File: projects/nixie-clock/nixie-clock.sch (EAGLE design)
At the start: 75 parts, among them J1 POWER JACK, T1 BC337, T2 BC337, T3 BC337, U1 Arduino Pro Mini, U2 K155ID1, U3 DC-DC Converter, U4 Pollin DCF1, U5 REG1117

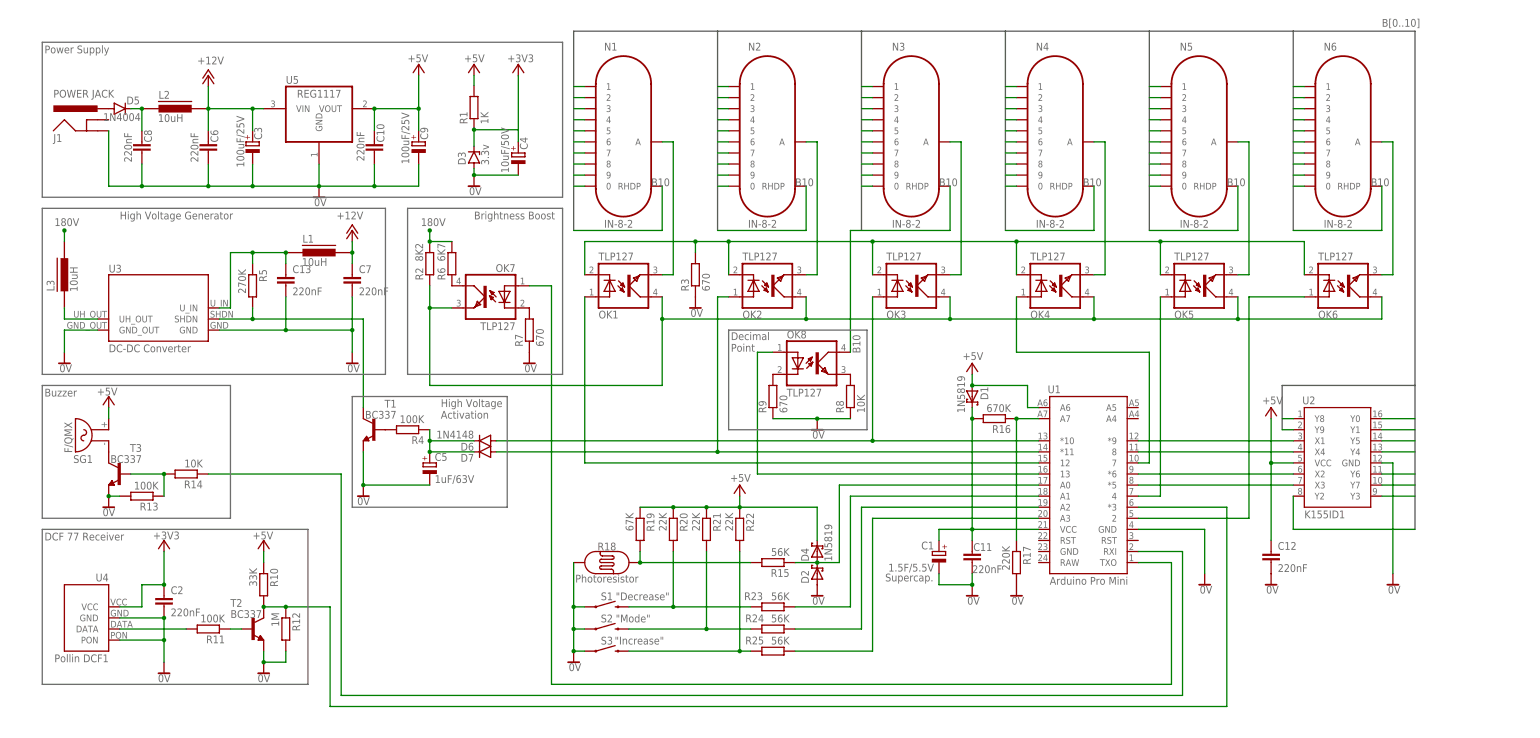
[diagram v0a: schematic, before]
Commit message: Renumber parts
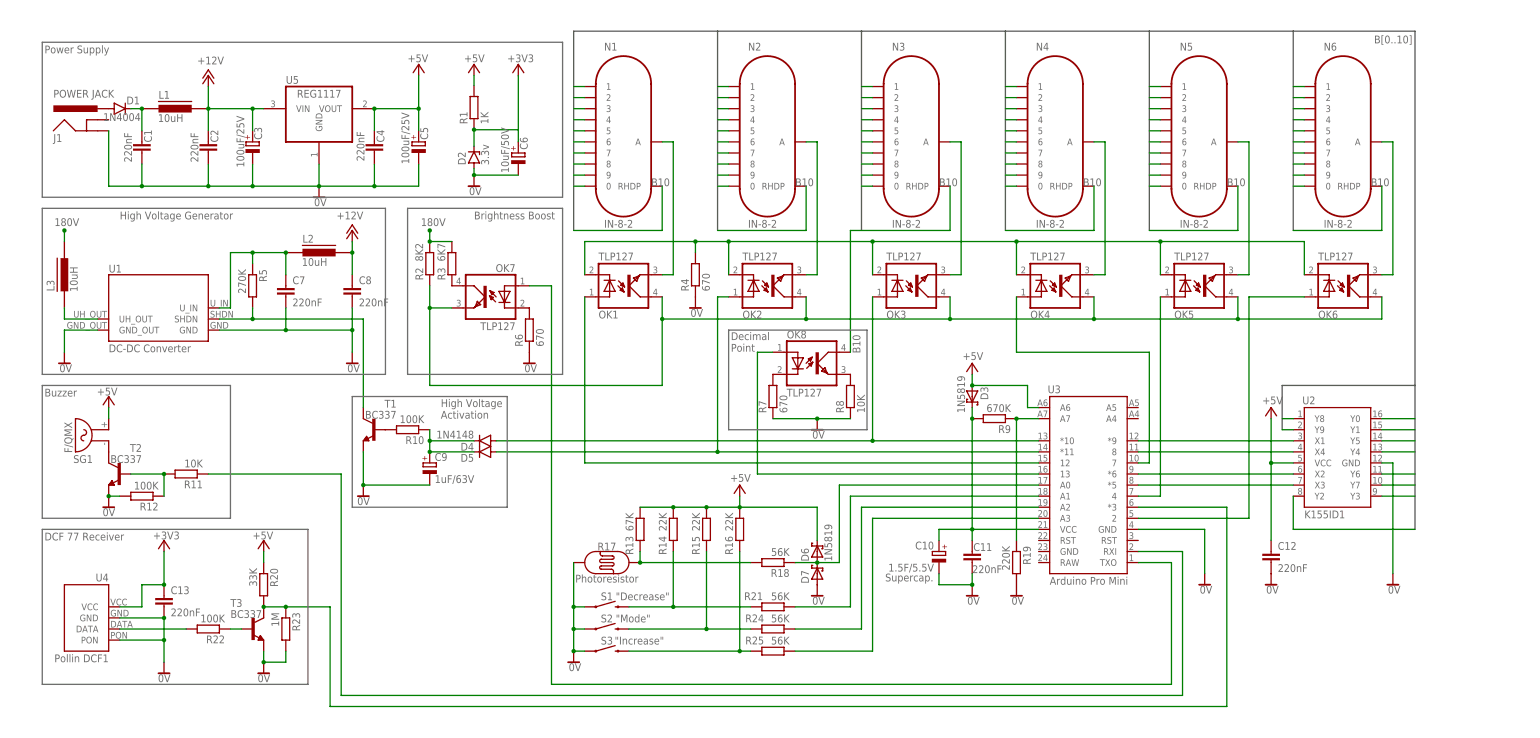
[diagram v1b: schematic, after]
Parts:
- C1: value 1.5F/5.5V -> 220nF; device karim:SUPERCAP/1.5F/5.5V -> rcl:C-EU025-024X044
- C10: value 220nF -> 1.5F/5.5V; device rcl:C-EU025-024X044 -> karim:SUPERCAP/1.5F/5.5V
- C4: value 10uF/50V -> 220nF; device rcl:CPOL-EUE2-4 -> rcl:C-EU025-024X044
- C5: value 1uF/63V -> 100uF/25V; device rcl:CPOL-EUE1.8-4 -> rcl:CPOL-EUE2.5-6
- C6: value 220nF -> 10uF/50V; device rcl:C-EU025-024X044 -> rcl:CPOL-EUE2-4
- C9: value 100uF/25V -> 1uF/63V; device rcl:CPOL-EUE2.5-6 -> rcl:CPOL-EUE1.8-4
- D1: value 1N5819 -> 1N4004; device diode:1N5819-B -> diode:1N4004
- D2: value 1N5819-B -> 3.3v; device diode:1N5819-B -> diode:ZENER-DIODEZD-5
- D3: value 3.3v -> 1N5819; device diode:ZENER-DIODEZD-5 -> diode:1N5819-B
- D4: value 1N5819 -> 1N4148; device diode:1N5819-B -> diode:1N4148DO35-7
- D5: value 1N4004 -> 1N4148; device diode:1N4004 -> diode:1N4148DO35-7
- D6: value 1N4148 -> 1N5819; device diode:1N4148DO35-7 -> diode:1N5819-B
- D7: value 1N4148 -> 1N5819-B; device diode:1N4148DO35-7 -> diode:1N5819-B
- R10: value 33K -> 100K
- R11: value 100K -> 10K
- R12: value 1M -> 100K
- R13: value 100K -> 67K
- R14: value 10K -> 22K
- R15: value 56K -> 22K
- R16: value 670K -> 22K
- R17: value 220K -> Photoresistor; device rcl:R-EU_0207/7 -> SparkFun-Sensors:PHOTOCELLPTH
- R18: value Photoresistor -> 56K; device SparkFun-Sensors:PHOTOCELLPTH -> rcl:R-EU_0207/7
- R19: value 67K -> 220K
- R20: value 22K -> 33K
- R21: value 22K -> 56K
- R22: value 22K -> 100K
- R23: value 56K -> 1M
- R3: value 670 -> 6K7
- R4: value 100K -> 670
- R6: value 6K7 -> 670
- R9: value 670 -> 670K
- U1: value Arduino Pro Mini -> DC-DC Converter; device karim:ARDUINO_PRO_MINI_TS -> karim:CHINA_HV_DC_DC
- U3: value DC-DC Converter -> Arduino Pro Mini; device karim:CHINA_HV_DC_DC -> karim:ARDUINO_PRO_MINI_TS
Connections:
- net +12V: now also C2.1, C8.1; no longer C6.1, C7.1
- net +3V3: now also C13.1, C6.+, D2.C; no longer C2.1, C4.+, D3.C
- net +5V: now also C4.1, C5.+, D3.A, D6.C, R13.1, R14.1, R15.1, R16.1, U3.A6; no longer C10.1, C9.+, D1.A, D4.C, R10.1, R19.1, R21.1, R22.1, U1.A6
- net 0V: now also C1.2, C10.-, C4.2, C6.-, D7.A, R17.P$1, R19.2, R23.2, R4.1, R6.1, U1.GND_OUT; no longer C1.-, C10.2, C4.-, C6.2, D3.A, R13.2, R17.2, R18.P$1, R3.1, R9.1, U3.GND_OUT
- net 180V: now also R3.2; no longer R6.2
- net 180VRAW: now also U1.UH_OUT; no longer U3.UH_OUT
- net N$10: now also U3.4; no longer U1.4
- net N$11: now also U3.7; no longer U1.7
- net N$12: now also D4.A, U3.*10; no longer D6.A, U1.*10
- net N$13: now also D5.A, U3.*11; no longer D7.A, U1.*11
- net N$14: now also U3.12; no longer U1.12
- net N$15: now also C7.1, L2.1, U1.U_IN; no longer C13.1, L1.1, U3.U_IN
- net N$16: now also R10.2; no longer R4.2
- net N$17: now also C9.+, D4.C, D5.C, R10.1; no longer C5.+, D6.C, D7.C, R4.1
- net N$18: now also U1.SHDN; no longer U3.SHDN
- net N$19: now also R4.2; no longer R3.2
- net N$20: now also R6.2; no longer R7.2
- net N$21: now also U3.TXO; no longer U1.TXO
- net N$23: now also R7.2; no longer R9.2
- net N$24: now also U3.13; no longer U1.13
- net N$25: now also D1.A; no longer D5.A
- net N$26: now also C1.1, D1.C, L1.1; no longer C8.1, D5.C, L2.1
- net N$27: now also R20.2, R23.1, T3.C, U3.*3; no longer R10.2, R12.1, T2.C, U1.*3
- net N$28: now also R11.2, R12.1, T2.B; no longer R13.1, R14.2, T3.B
- net N$29: now also R22.1, T3.B; no longer R11.1, T2.B
- net N$30: now also R22.2; no longer R11.2
- net N$31: now also T2.C; no longer T3.C
- net N$32: now also R11.1, U3.RXI; no longer R14.1, U1.RXI
- net N$33: now also C10.+, D3.C, R9.2, U3.VCC; no longer C1.+, D1.C, R16.2, U1.VCC
- net N$34: now also R19.1, R9.1, U3.A7; no longer R16.1, R17.1, U1.A7
- net N$35: now also D6.A, D7.C, R18.1, U3.A0; no longer D2.C, D4.A, R15.1, U1.A0
- net N$36: now also R13.2, R17.P$2, R18.2; no longer R15.2, R18.P$2, R19.2
- net N$37: now also R14.2, R21.2; no longer R20.2, R23.2
- net N$38: now also R15.2; no longer R21.2
- net N$39: now also R16.2; no longer R22.2
- net N$40: now also R21.1, U3.A1; no longer R23.1, U1.A1
- net N$41: now also U3.A2; no longer U1.A2
- net N$42: now also U3.A3; no longer U1.A3
- net N$8: now also R3.1; no longer R6.1
- net N$9: now also U3.2; no longer U1.2
- net X1: now also U3.*9; no longer U1.*9
- net X2: now also U3.*6; no longer U1.*6
- net X3: now also U3.*5; no longer U1.*5
- net X4: now also U3.8; no longer U1.8
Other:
- moved on the sheet: C13, C2, C5, C7, C8, C9, L1, L2, R10, R11, R12, R13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

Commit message: Added copyright notice
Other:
- note added: "Copyright © 2018, Karim Hraibi Please visit: www.microfarad.de/nixie-clock www.github.com/microfarad-de/nixie-clock"
- note added: "Nixie Clock"
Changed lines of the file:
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@@
 <text x="-17.272" y="22.352" size="1.778" layer="95" align="top-left">Decimal
 Point</text>
+<text x="86.36" y="-40.64" size="3.81" layer="95" align="top-left">Nixie Clock</text>
+<text x="86.36" y="-48.26" size="2.1844" layer="95" align="top-left">Copyright © 2018, Karim Hraibi
+Please visit:
+www.microfarad.de/nixie-clock
+www.github.com/microfarad-de/nixie-clock</text>
 </plain>
 <instances>
@@
 <attribute name="VALUE" x="-105.283" y="13.208" size="1.778" layer="96"/>
 </instance>
-<instance part="SUPPLY10" gate="0V" x="91.44" y="-35.56" smashed="yes">
-<attribute name="VALUE" x="90.297" y="-37.592" size="1.778" layer="96"/>
+<instance part="SUPPLY10" gate="0V" x="81.28" y="-35.56" smashed="yes">
+<attribute name="VALUE" x="80.137" y="-37.592" size="1.778" layer="96"/>
 </instance>
 <instance part="P+5" gate="1" x="38.1" y="15.24" smashed="yes">
@@
 </instance>
 <instance part="J1" gate="G$1" x="-162.56" y="66.04" smashed="yes">
-<attribute name="VALUE" x="-172.72" y="76.2" size="1.778" layer="96" font="vector"/>
+<attribute name="VALUE" x="-172.72" y="76.2" size="1.778" layer="96"/>
 <attribute name="NAME" x="-172.72" y="66.04" size="1.778" layer="95" font="vector"/>
 </instance>
@@
 <segment>
 <pinref part="U3" gate="G$1" pin="GND"/>
-<wire x1="76.2" y1="-22.86" x2="91.44" y2="-22.86" width="0.1524" layer="91"/>
+<wire x1="76.2" y1="-22.86" x2="81.28" y2="-22.86" width="0.1524" layer="91"/>
 <pinref part="SUPPLY10" gate="0V" pin="0V"/>
-<wire x1="91.44" y1="-22.86" x2="91.44" y2="-33.02" width="0.1524" layer="91"/>
+<wire x1="81.28" y1="-22.86" x2="81.28" y2="-33.02" width="0.1524" layer="91"/>
 </segment>
 <segment>
@@
 <segment>
 <pinref part="U3" gate="G$1" pin="TXO"/>
-<wire x1="76.2" y1="-30.48" x2="83.82" y2="-30.48" width="0.1524" layer="91"/>
-<wire x1="83.82" y1="-30.48" x2="83.82" y2="-58.42" width="0.1524" layer="91"/>
-<wire x1="83.82" y1="-58.42" x2="-58.42" y2="-58.42" width="0.1524" layer="91"/>
+<wire x1="76.2" y1="-30.48" x2="76.2" y2="-58.42" width="0.1524" layer="91"/>
+<wire x1="76.2" y1="-58.42" x2="-58.42" y2="-58.42" width="0.1524" layer="91"/>
 <pinref part="OK7" gate="G$1" pin="A"/>
 <wire x1="-58.42" y1="-58.42" x2="-58.42" y2="33.02" width="0.1524" layer="91"/>
@@
 <net name="N$27" class="0">
 <segment>
-<wire x1="-109.22" y1="-63.5" x2="96.52" y2="-63.5" width="0.1524" layer="91"/>
+<wire x1="-109.22" y1="-63.5" x2="83.82" y2="-63.5" width="0.1524" layer="91"/>
 <pinref part="T3" gate="G$1" pin="C"/>
 <pinref part="R20" gate="G$1" pin="2"/>
@@
 <junction x="-119.38" y="-40.64"/>
 <pinref part="U3" gate="G$1" pin="*3"/>
-<wire x1="96.52" y1="-63.5" x2="96.52" y2="-17.78" width="0.1524" layer="91"/>
-<wire x1="96.52" y1="-17.78" x2="76.2" y2="-17.78" width="0.1524" layer="91"/>
+<wire x1="83.82" y1="-63.5" x2="83.82" y2="-17.78" width="0.1524" layer="91"/>
+<wire x1="83.82" y1="-17.78" x2="76.2" y2="-17.78" width="0.1524" layer="91"/>
 </segment>
 </net>
@@
 <wire x1="-137.16" y1="-10.16" x2="-106.68" y2="-10.16" width="0.1524" layer="91"/>
 <wire x1="-106.68" y1="-10.16" x2="-106.68" y2="-60.96" width="0.1524" layer="91"/>
-<wire x1="-106.68" y1="-60.96" x2="86.36" y2="-60.96" width="0.1524" layer="91"/>
-<wire x1="86.36" y1="-60.96" x2="86.36" y2="-27.94" width="0.1524" layer="91"/>
+<wire x1="-106.68" y1="-60.96" x2="78.74" y2="-60.96" width="0.1524" layer="91"/>
+<wire x1="78.74" y1="-60.96" x2="78.74" y2="-27.94" width="0.1524" layer="91"/>
 <pinref part="U3" gate="G$1" pin="RXI"/>
-<wire x1="86.36" y1="-27.94" x2="76.2" y2="-27.94" width="0.1524" layer="91"/>
-</segment>
-</net>
+<wire x1="78.74" y1="-27.94" x2="76.2" y2="-27.94" width="0.1524" layer="91"/>
+</segment>
+</net>

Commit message: Update schematic
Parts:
- removed R12: 100K, rcl:R-EU_0207/7
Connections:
- net 0V: no longer R12.2
- net N$28: no longer R12.1
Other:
- moved on the sheet: R11
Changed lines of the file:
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@@
 <part name="D7" library="diode" library_urn="urn:adsk.eagle:library:210" deviceset="1N581*" device="" package3d_urn="urn:adsk.eagle:package:43421/1" technology="9-B"/>
 <part name="SUPPLY13" library="supply2" library_urn="urn:adsk.eagle:library:372" deviceset="0V" device=""/>
-<part name="R12" library="rcl" library_urn="urn:adsk.eagle:library:334" deviceset="R-EU_" device="0207/7" package3d_urn="urn:adsk.eagle:package:23493/2" value="100K"/>
 </parts>
 <sheets>
@@
 www.microfarad.de/nixie-clock
 www.github.com/microfarad-de/nixie-clock</text>
+<wire x1="-180.34" y1="96.52" x2="144.78" y2="96.52" width="0.1524" layer="95"/>
+<wire x1="144.78" y1="96.52" x2="144.78" y2="-68.58" width="0.1524" layer="95"/>
+<wire x1="144.78" y1="-68.58" x2="-182.88" y2="-68.58" width="0.1524" layer="95"/>
+<wire x1="-182.88" y1="-68.58" x2="-180.34" y2="96.52" width="0.1524" layer="95"/>
 </plain>
 <instances>
@@
 <attribute name="VALUE" x="-152.4" y="-7.62" size="1.778" layer="96" rot="MR0"/>
 </instance>
-<instance part="R11" gate="G$1" x="-142.24" y="-10.16" smashed="yes" rot="R180">
-<attribute name="NAME" x="-138.43" y="-11.6586" size="1.778" layer="95" rot="R180"/>
-<attribute name="VALUE" x="-138.43" y="-6.858" size="1.778" layer="96" rot="R180"/>
+<instance part="R11" gate="G$1" x="-144.78" y="-10.16" smashed="yes" rot="R180">
+<attribute name="NAME" x="-140.97" y="-11.6586" size="1.778" layer="95" rot="R180"/>
+<attribute name="VALUE" x="-140.97" y="-6.858" size="1.778" layer="96" rot="R180"/>
 </instance>
 <instance part="SUPPLY9" gate="0V" x="-160.02" y="-17.78" smashed="yes" rot="MR0">
@@
 <instance part="SUPPLY13" gate="0V" x="2.54" y="-38.1" smashed="yes">
 <attribute name="VALUE" x="1.397" y="-40.132" size="1.778" layer="96"/>
-</instance>
-<instance part="R12" gate="G$1" x="-152.4" y="-15.24" smashed="yes" rot="R180">
-<attribute name="NAME" x="-148.59" y="-16.7386" size="1.778" layer="95" rot="R180"/>
-<attribute name="VALUE" x="-148.59" y="-11.938" size="1.778" layer="96" rot="R180"/>
 </instance>
 </instances>
@@
 <pinref part="T2" gate="G$1" pin="E"/>
 <pinref part="SUPPLY9" gate="0V" pin="0V"/>
-<pinref part="R12" gate="G$1" pin="2"/>
-<wire x1="-157.48" y1="-15.24" x2="-160.02" y2="-15.24" width="0.1524" layer="91"/>
-<junction x="-160.02" y="-15.24"/>
 </segment>
 <segment>
@@
 <segment>
 <pinref part="R11" gate="G$1" pin="1"/>
-<wire x1="-137.16" y1="-10.16" x2="-106.68" y2="-10.16" width="0.1524" layer="91"/>
+<wire x1="-139.7" y1="-10.16" x2="-106.68" y2="-10.16" width="0.1524" layer="91"/>
 <wire x1="-106.68" y1="-10.16" x2="-106.68" y2="-60.96" width="0.1524" layer="91"/>
 <wire x1="-106.68" y1="-60.96" x2="78.74" y2="-60.96" width="0.1524" layer="91"/>
@@
 <pinref part="R11" gate="G$1" pin="2"/>
 <pinref part="T2" gate="G$1" pin="B"/>
-<wire x1="-147.32" y1="-10.16" x2="-154.94" y2="-10.16" width="0.1524" layer="91"/>
-<wire x1="-147.32" y1="-15.24" x2="-147.32" y2="-10.16" width="0.1524" layer="91"/>
-<junction x="-147.32" y="-10.16"/>
-<pinref part="R12" gate="G$1" pin="1"/>
-</segment>
-</net>
+<wire x1="-149.86" y1="-10.16" x2="-154.94" y2="-10.16" width="0.1524" layer="91"/>
+</segment>
+</net>

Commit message: Update nixie-clock schematic
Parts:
- J1: value POWER JACK -> Power Jack
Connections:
- net 180V renamed +180V
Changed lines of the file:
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@@
 <part name="R7" library="rcl" library_urn="urn:adsk.eagle:library:334" deviceset="R-EU_" device="0207/7" package3d_urn="urn:adsk.eagle:package:23493/2" value="670"/>
 <part name="SUPPLY7" library="supply2" library_urn="urn:adsk.eagle:library:372" deviceset="0V" device=""/>
-<part name="J1" library="SparkFun-Connectors" library_urn="urn:adsk.eagle:library:513" deviceset="POWER_JACK" device="SLT" package3d_urn="urn:adsk.eagle:package:38222/1" value="POWER JACK"/>
+<part name="J1" library="SparkFun-Connectors" library_urn="urn:adsk.eagle:library:513" deviceset="POWER_JACK" device="SLT" package3d_urn="urn:adsk.eagle:package:38222/1" value="Power Jack"/>
 <part name="D1" library="diode" library_urn="urn:adsk.eagle:library:210" deviceset="1N4004" device="" package3d_urn="urn:adsk.eagle:package:43336/1"/>
 <part name="+3V32" library="supply1" library_urn="urn:adsk.eagle:library:371" deviceset="+3V3" device=""/>
@@
 </segment>
 </net>
-<net name="180V" class="0">
+<net name="+180V" class="0">
 <segment>
 <pinref part="L3" gate="G$1" pin="2"/>
